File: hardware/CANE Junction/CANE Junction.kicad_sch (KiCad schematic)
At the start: 28 parts, among them IC1 PAM8904QJER, J3 programming, J4 UART, SW101 SW_Push, U1 MX25L3233FM2, U102 NCP114ASN180T2G, U2 XMSPM0G3519SPMR

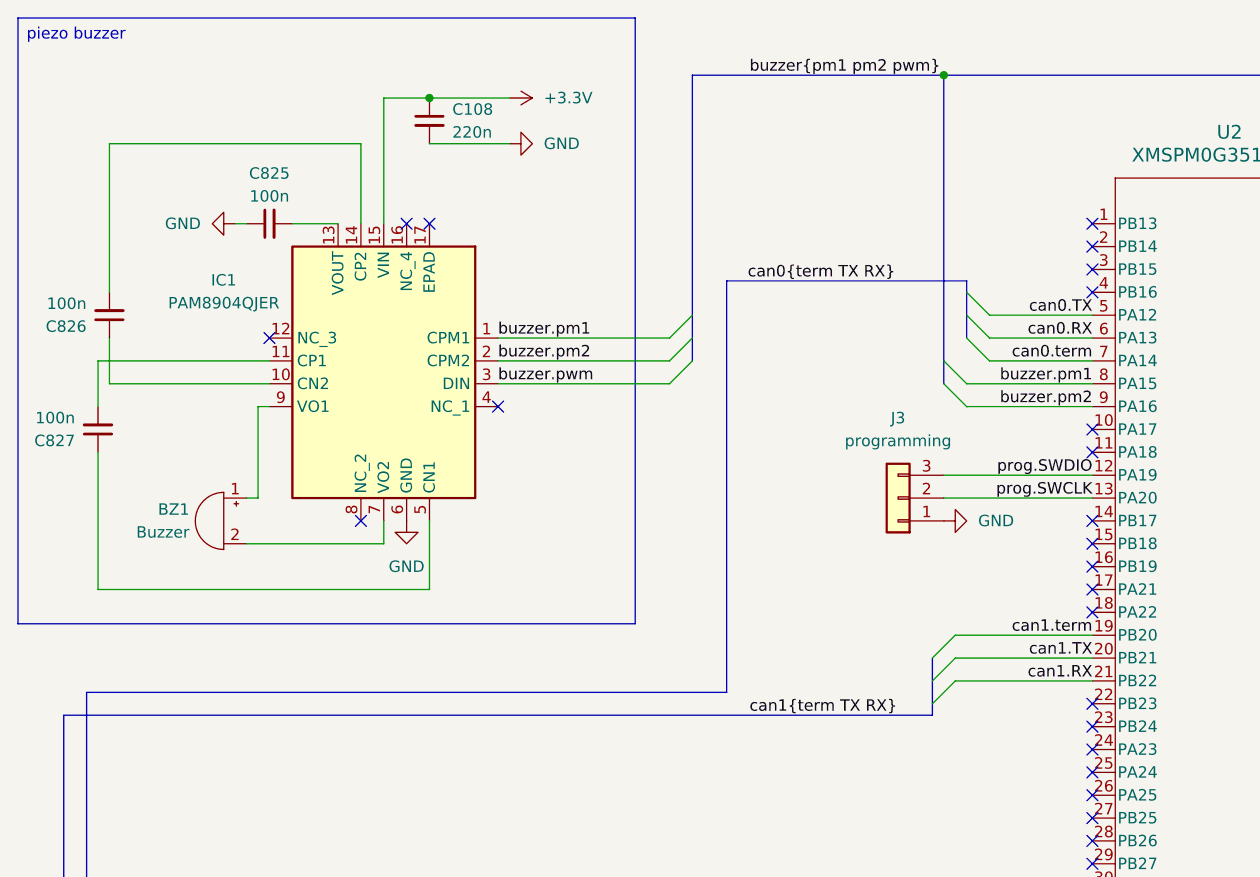
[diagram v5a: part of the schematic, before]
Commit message: transcevier out of stock, swapped out
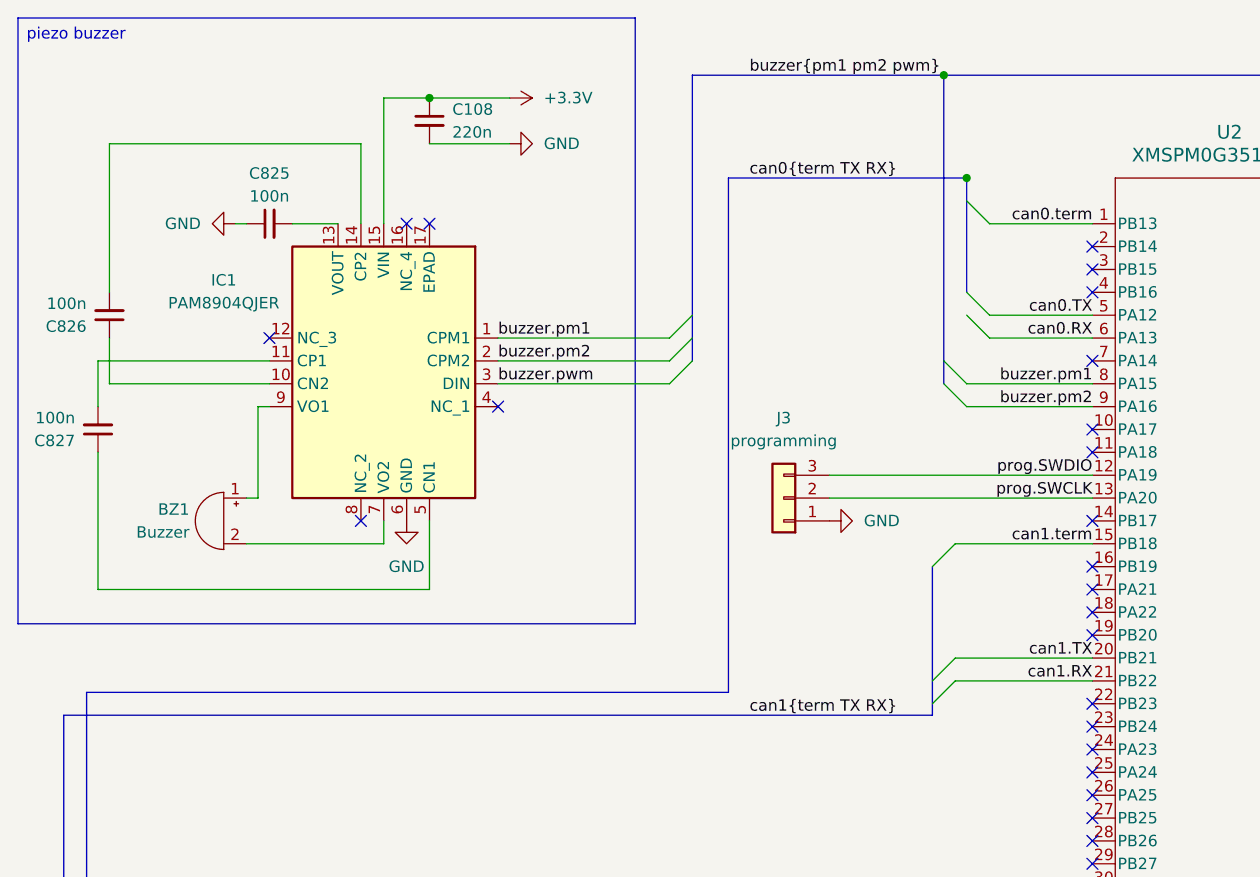
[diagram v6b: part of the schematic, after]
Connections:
- net can0.term: now also U2.1 (PB13); no longer U2.7 (PA14)
- net can1.term: now also U2.15 (PB18); no longer U2.19 (PB20)
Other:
- moved on the sheet: J3
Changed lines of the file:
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@@
 	)
 	(junction
+		(at 118.11 33.02)
+		(diameter 0)
+		(color 0 0 0 0)
+	)
+	(junction
 		(at 176.53 104.14)
 		(diameter 0)
@@
 	)
 	(no_connect
-		(at 132.08 73.66)
-	)
-	(no_connect
 		(at 132.08 40.64)
 	)
@@
 	)
 	(no_connect
-		(at 132.08 71.12)
-	)
-	(no_connect
 		(at 132.08 45.72)
 	)
@@
 	)
 	(no_connect
+		(at 132.08 83.82)
+	)
+	(no_connect
 		(at 162.56 114.3)
 	)
@@
 	)
 	(no_connect
-		(at 132.08 38.1)
-	)
-	(no_connect
 		(at 162.56 91.44)
 	)
@@
 	)
 	(no_connect
+		(at 132.08 53.34)
+	)
+	(no_connect
 		(at 132.08 106.68)
 	)
@@
 	)
 	(no_connect
+		(at 132.08 71.12)
+	)
+	(no_connect
 		(at 162.56 66.04)
 	)
@@
 	)
 	(bus_entry
+		(at 120.65 38.1)
+		(size -2.54 -2.54)
+		(stroke
+			(width 0)
+			(type default)
+		)
+	)
+	(bus_entry
 		(at 222.25 73.66)
 		(size 2.54 2.54)
@@
 	)
 	(bus_entry
-		(at 114.3 86.36)
-		(size 2.54 -2.54)
-		(stroke
-			(width 0)
-			(type default)
-		)
-	)
-	(bus_entry
 		(at 222.25 78.74)
 		(size 2.54 2.54)
@@
 	)
 	(bus_entry
-		(at 120.65 53.34)
-		(size -2.54 -2.54)
-		(stroke
-			(width 0)
-			(type default)
-		)
-	)
-	(bus_entry
 		(at 191.77 43.18)
 		(size -2.54 2.54)
@@
 	)
 	(bus_entry
+		(at 114.3 76.2)
+		(size 2.54 -2.54)
+		(stroke
+			(width 0)
+			(type default)
+		)
+	)
+	(bus_entry
 		(at 20.32 153.67)
 		(size 2.54 2.54)
@@
 	(bus
 		(pts
-			(xy 114.3 86.36) (xy 114.3 92.71)
+			(xy 114.3 76.2) (xy 114.3 92.71)
 		)
 		(stroke
@@
 	(bus
 		(pts
-			(xy 91.44 44.45) (xy 118.11 44.45)
+			(xy 91.6391 33.02) (xy 118.11 33.02)
 		)
 		(stroke
@@
 	(wire
 		(pts
-			(xy 115.57 66.04) (xy 132.08 66.04)
+			(xy 102.87 66.04) (xy 132.08 66.04)
 		)
 		(stroke
@@
 		)
 	)
-	(bus
+	(wire
 		(pts
-			(xy 118.11 44.45) (xy 118.11 50.8)
+			(xy 179.07 116.84) (xy 181.61 116.84)
 		)
 		(stroke
@@
 		)
 	)
-	(wire
+	(bus
 		(pts
-			(xy 179.07 116.84) (xy 181.61 116.84)
+			(xy 118.11 33.02) (xy 118.3091 33.02)
 		)
 		(stroke
@@
 		)
 	)
+	(bus
+		(pts
+			(xy 118.11 33.02) (xy 118.11 45.72)
+		)
+		(stroke
+			(width 0)
+			(type default)
+		)
+	)
 	(wire
 		(pts
@@
 	(wire
 		(pts
-			(xy 40.64 53.34) (xy 21.59 53.34)
+			(xy 120.65 38.1) (xy 132.08 38.1)
 		)
 		(stroke
@@
 	(wire
 		(pts
-			(xy 162.56 86.36) (xy 189.23 86.36)
+			(xy 40.64 53.34) (xy 21.59 53.34)
 		)
 		(stroke
@@
 	(wire
 		(pts
-			(xy 119.38 116.84) (xy 129.54 116.84)
+			(xy 162.56 86.36) (xy 189.23 86.36)
 		)
 		(stroke
@@
 		)
 	)
-	(bus
+	(wire
 		(pts
-			(xy 115.57 53.34) (xy 115.57 55.88)
+			(xy 119.38 116.84) (xy 129.54 116.84)
 		)
 		(stroke
@@
 		)
 	)
-	(wire
+	(bus
 		(pts
-			(xy 116.84 83.82) (xy 132.08 83.82)
+			(xy 115.57 53.34) (xy 115.57 55.88)
 		)
 		(stroke
@@
 	(wire
 		(pts
-			(xy 115.57 68.58) (xy 132.08 68.58)
+			(xy 102.87 68.58) (xy 132.08 68.58)
 		)
 		(stroke
@@
 	(bus
 		(pts
-			(xy 91.44 90.17) (xy 20.32 90.17)
+			(xy 91.6391 90.17) (xy 20.32 90.17)
 		)
 		(stroke
@@
 		)
 	)
+	(wire
+		(pts
+			(xy 116.84 73.66) (xy 132.08 73.66)
+		)
+		(stroke
+			(width 0)
+			(type default)
+		)
+	)
 	(bus
 		(pts
@@
 	(bus
 		(pts
-			(xy 91.44 44.45) (xy 91.44 90.17)
+			(xy 91.6391 33.02) (xy 91.6391 90.17)
 		)
 		(stroke
@@
 	(wire
 		(pts
-			(xy 120.65 53.34) (xy 132.08 53.34)
-		)
-		(stroke
-			(width 0)
-			(type default)
-		)
-	)
-	(wire
-		(pts
 			(xy 187.96 93.98) (xy 176.53 93.98)
 		)
@@
 		)
 	)
+	(label "can0.term"
+		(at 132.08 38.1 180)
+		(effects
+			(font
+				(size 1.27 1.27)
+			)
+			(justify right bottom)
+		)
+	)
 	(label "buzzer.pm2"
 		(at 132.08 58.42 180)
@@
 		)
 	)
-	(label "can0.term"
-		(at 132.08 53.34 180)
-		(effects
-			(font
-				(size 1.27 1.27)
-			)
-			(justify right bottom)
-		)
-	)
 	(label "can1{term TX RX}"
 		(at 93.98 92.71 0)
@@
 		)
 	)
+	(label "can1.term"
+		(at 132.08 73.66 180)
+		(effects
+			(font
+				(size 1.27 1.27)
+			)
+			(justify right bottom)
+		)
+	)
 	(label "eth.MISO{slash}POCI"
 		(at 162.56 50.8 0)
@@
 	)
 	(label "can0{term TX RX}"
-		(at 93.7809 44.45 0)
+		(at 93.98 33.02 0)
 		(effects
 			(font
@@
 		)
 	)
-	(label "can1.term"
-		(at 132.08 83.82 180)
-		(effects
-			(font
-				(size 1.27 1.27)
-			)
-			(justify right bottom)
-		)
-	)
 	(symbol
 		(lib_id "power:+3.3V")
@@
 	(symbol
 		(lib_id "power:GND")
-		(at 115.57 71.12 90)
+		(at 102.87 71.12 90)
 		(unit 1)
 		(body_style 1)
@@
 		(fields_autoplaced yes)
 		(property "Reference" "#PWR0118"
-			(at 121.92 71.12 0)
+			(at 109.22 71.12 0)
 			(hide yes)
 			(show_name no)
@@
 		)
 		(property "Value" "GND"
-			(at 119.38 71.1199 90)
+			(at 106.68 71.1199 90)
 			(show_name no)
 			(do_not_autoplace no)
@@
 		)
 		(property "Footprint" ""
-			(at 115.57 71.12 0)
+			(at 102.87 71.12 0)
 			(hide yes)
 			(show_name no)
@@
 		)
 		(property "Datasheet" ""
-			(at 115.57 71.12 0)
+			(at 102.87 71.12 0)
 			(hide yes)
 			(show_name no)
@@
 		)
 		(property "Description" "Power symbol creates a global label with name \"GND\" , ground"
-			(at 115.57 71.12 0)
+			(at 102.87 71.12 0)
 			(hide yes)
 			(show_name no)
@@
 	(symbol
 		(lib_id "Connector_Generic:Conn_01x03")
-		(at 110.49 68.58 180)
+		(at 97.79 68.58 180)
 		(unit 1)
 		(body_style 1)
@@
 		(fields_autoplaced yes)
 		(property "Reference" "J3"
-			(at 110.49 59.69 0)
+			(at 97.79 59.69 0)
 			(show_name no)
 			(do_not_autoplace no)
@@
 		)
 		(property "Value" "programming"
-			(at 110.49 62.23 0)
+			(at 97.79 62.23 0)
 			(show_name no)
 			(do_not_autoplace no)
@@
 		)
 		(property "Footprint" "Connector_PinHeader_2.54mm:PinHeader_1x03_P2.54mm_Vertical"
-			(at 110.49 68.58 0)
+			(at 97.79 68.58 0)
 			(hide yes)
 			(show_name no)
@@
 		)
 		(property "Datasheet" ""
-			(at 110.49 68.58 0)
+			(at 97.79 68.58 0)
 			(hide yes)
 			(show_name no)
@@
 		)
 		(property "Description" "Generic connector, single row, 01x03, script generated (kicad-library-utils/schlib/autogen/connector/)"
-			(at 110.49 68.58 0)
+			(at 97.79 68.58 0)
 			(hide yes)
 			(show_name no)

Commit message: mmm
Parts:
- removed C103, C104: 220n, Capacitor_SMD:C_0805_2012Metric_Pad1.18x1.45mm_HandSolder, symbol Device:C_Small
- removed R2: 40.2k, Resistor_SMD:R_0805_2012Metric_Pad1.20x1.40mm_HandSolder, symbol Device:R_Small_US
- added C1: 470n, Capacitor_SMD:C_0805_2012Metric_Pad1.18x1.45mm_HandSolder, symbol Device:C_Small
- added R1: 100k, Resistor_SMD:R_0805_2012Metric_Pad1.20x1.40mm_HandSolder, symbol Device:R_Small_US
- added TP1: TestPoint, TestPoint:TestPoint_Pad_D1.0mm, symbol Connector:TestPoint
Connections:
- net +3.3V: now also R1.1
- net GND: now also C1.2
- net at U2.32 (VCORE): now also C1.1
- net at SW101.1, U2.38 (NRST): now also R1.2
- net at C105.1, D1.1 (K), D2.1 (K)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: now also TP1.1
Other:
- moved on the sheet: C107

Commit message: tmb pci technology
doner motherboard generator
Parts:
- removed C102, C105, C108, C109: 220n, Capacitor_SMD:C_0805_2012Metric_Pad1.18x1.45mm_HandSolder, symbol Device:C_Small
- removed C825, C826, C827: 100n, Capacitor_SMD:C_0805_2012Metric_Pad1.18x1.45mm_HandSolder, symbol Device:C_Small
- removed D1, D2: SD0805S020S1R0, Diode_SMD:D_0805_2012Metric_Pad1.15x1.40mm_HandSolder, symbol Device:D_Schottky_Small
- removed TP1: TestPoint, TestPoint:TestPoint_Pad_D1.0mm, symbol Connector:TestPoint
- removed U102: NCP114ASN180T2G, Package_TO_SOT_SMD:SOT-23-5_HandSoldering, symbol Regulator_Linear:NCP163ASN330T1G
- added C10, C8, C9: 100n, Capacitor_SMD:C_0805_2012Metric_Pad1.18x1.45mm_HandSolder, symbol Device:C_Small
- added C11, C2, C3: 470n, Capacitor_SMD:C_0805_2012Metric_Pad1.18x1.45mm_HandSolder, symbol Device:C_Small
- added C5, C7: 22u, Capacitor_SMD:C_0805_2012Metric_Pad1.18x1.45mm_HandSolder, symbol Device:C_Small
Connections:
- net +3.3V: now also R103.1, C11.1, C3.1, C5.2, C7.1
- net GND: now also U2.56 (PA10), C11.2, C2.2, C3.2, C5.1, C7.2, C8.1; no longer D102.1 (K)
- net SECD.cs_fr: now also U2.43 (PA3); no longer U2.48 (PB1)
- net can1.term: now also U2.11 (PA18); no longer U2.15 (PB18)
- net eth.irq_N: now also U2.58 (PB6)
- net eth.reset_N: now also U2.57 (PA11); no longer U2.58 (PB6)
- net at C1.1, U2.32 (VCORE): now also C2.1
- net at U2.33 (PA0): now also D102.1 (K); no longer R103.1
- net at IC1.13 (VOUT): now also C8.2
- net at IC1.10 (CN2): now also C9.2
- net at IC1.14 (CP2): now also C9.1
- net at IC1.5 (CN1): now also C10.2
- net at IC1.11 (CP1): now also C10.1
- no-connect marks 40 -> 37
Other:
- sheet CAN interface 1 ports: added 3v3; removed 5v
- sheet CAN interface 2 ports: added 3v3; removed 5v
- moved on the sheet: D102, J3, R103
